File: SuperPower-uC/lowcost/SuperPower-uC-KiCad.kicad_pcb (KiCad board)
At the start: 2 copper layers, 81 x 28.5 mm, 81 parts, among them J1 Battery connector, J2 Thermistor, J3 USB_B_Micro, J4 Solar in, J5 main pin header fight, J6 main pin header left, Q1 2N7002, Q2 2N7002, Q3 S8050, Q4 S8050, Q5 AO3401A, Q6 AO3401A, Q7 2N7002, U1 FS312F-G, U10 FP6291LR, U11 ME6210A33P, U12 ME6210A33P, U13 ESP32-WROOM32, U2 FS8205A, U3 LC709203FQH, U4 TP4056, U5 CH340G, U6 AMS1117-3.3, U7 PCF8563T, U8 XC6206P332MR, U9 TCA6408A, Y1 12MHZ, Y2 32.768KHz

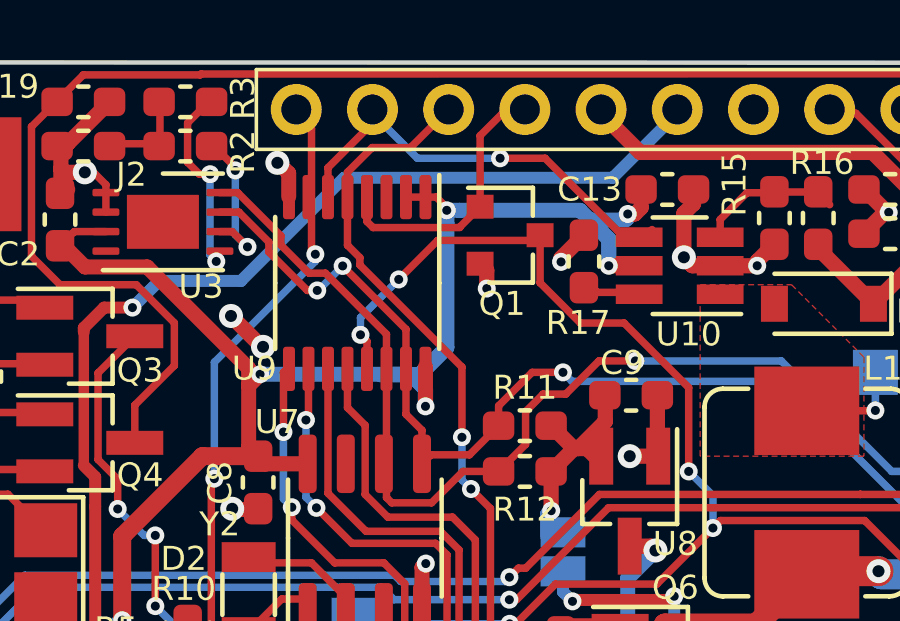
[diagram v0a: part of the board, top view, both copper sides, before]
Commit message: added pullup to pcb
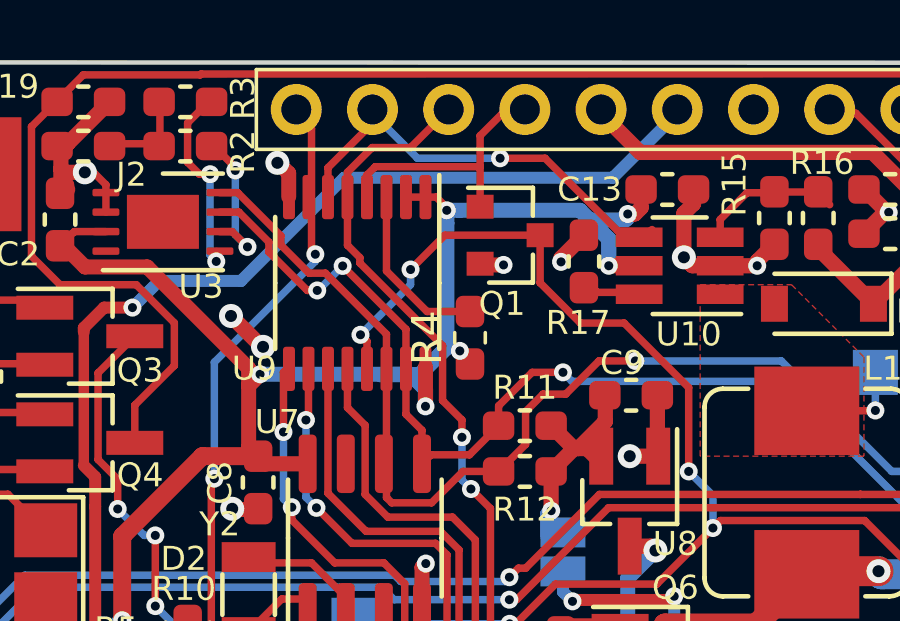
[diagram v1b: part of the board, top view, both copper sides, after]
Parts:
- added R4: 180k, Resistor_SMD:R_0603_1608Metric_Pad1.05x0.95mm_HandSolder, F.Cu at (136.5, 104.1)
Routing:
- net Net-(R4-Pad2): track 0.00 -> 5.81 mm
- net /Battery Module/VBAT: track 119.6 -> 120.6 mm, vias 15 -> 16

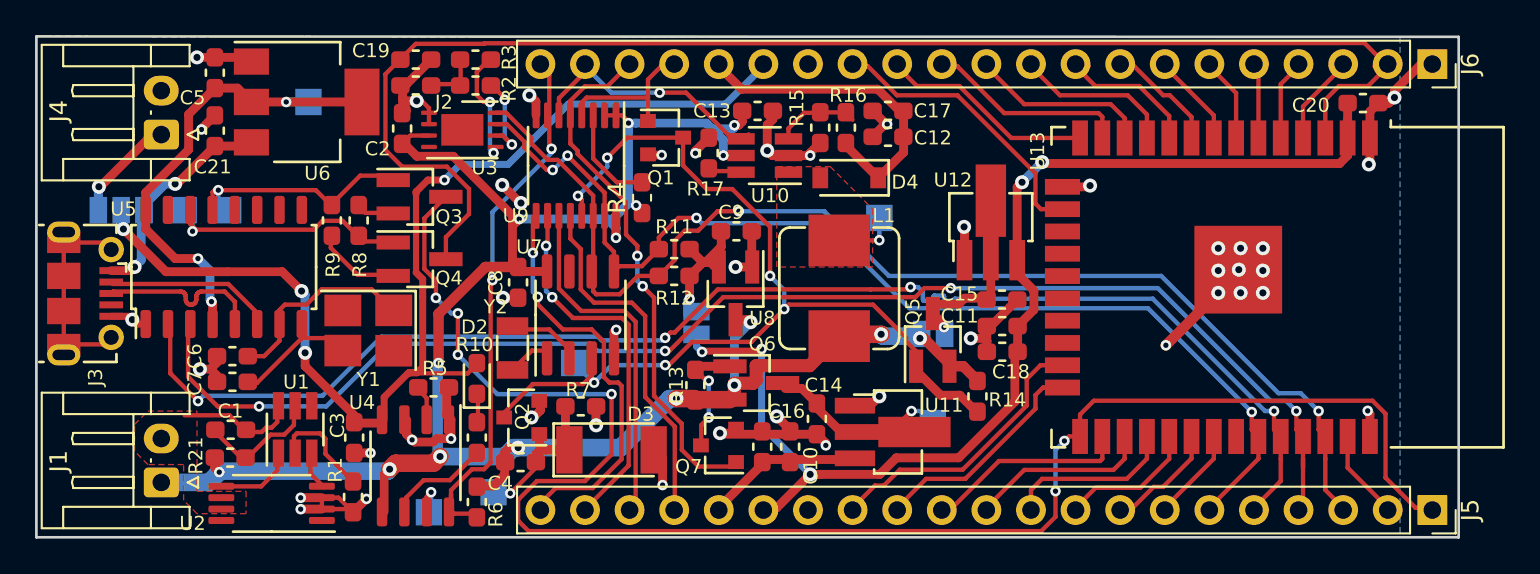
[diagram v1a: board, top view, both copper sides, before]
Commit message: connected vcci of io expander to vI2C
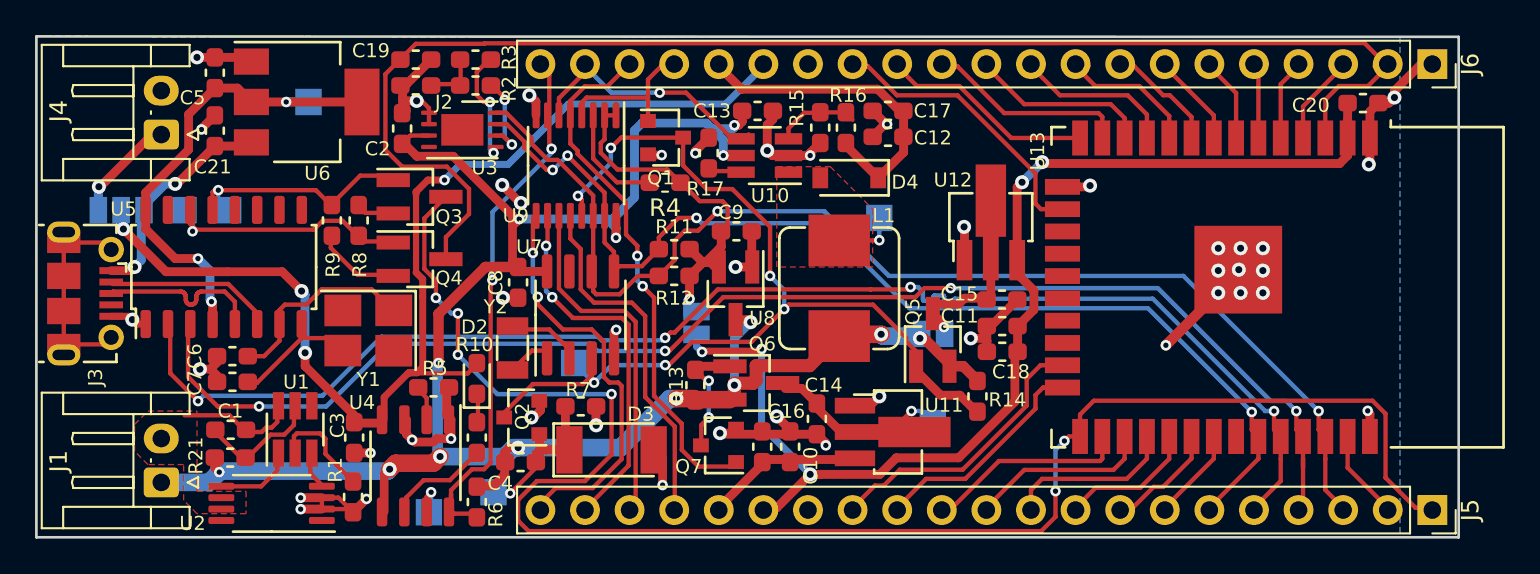
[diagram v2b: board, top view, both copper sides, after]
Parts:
- moved R4 1.56 mm to (137.8, 103.3), turned to 180 degrees
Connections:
- R4 pad 1: /Battery Module/VBAT -> /RTC and Cut-Off Module/V_I2C
- U9 pad 1: /Battery Module/VBAT -> /RTC and Cut-Off Module/V_I2C
- U9 pad 2: /Battery Module/VBAT -> /RTC and Cut-Off Module/V_I2C
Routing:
- net /RTC and Cut-Off Module/V_I2C: track 7.44 -> 20.4 mm
- net /Battery Module/VBAT: track 120.6 -> 117.5 mm, vias 16 -> 14

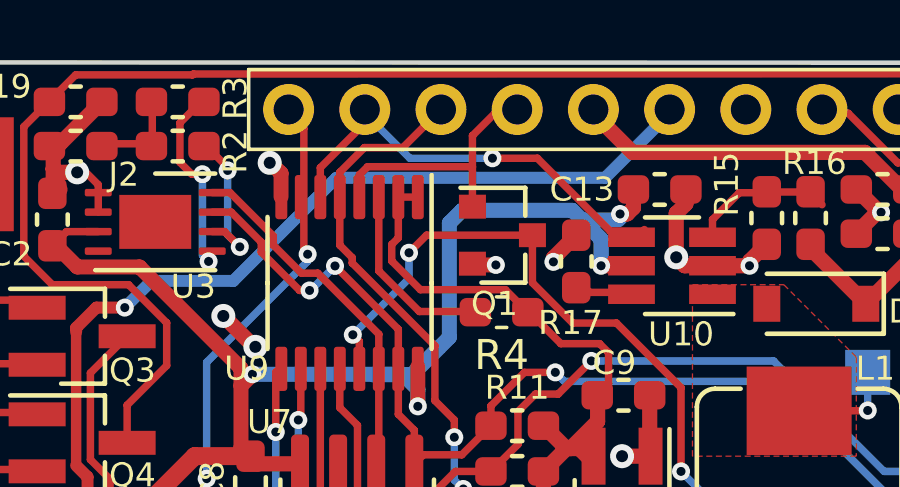
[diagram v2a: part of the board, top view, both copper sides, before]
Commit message: changed int io to directely connect to int bus
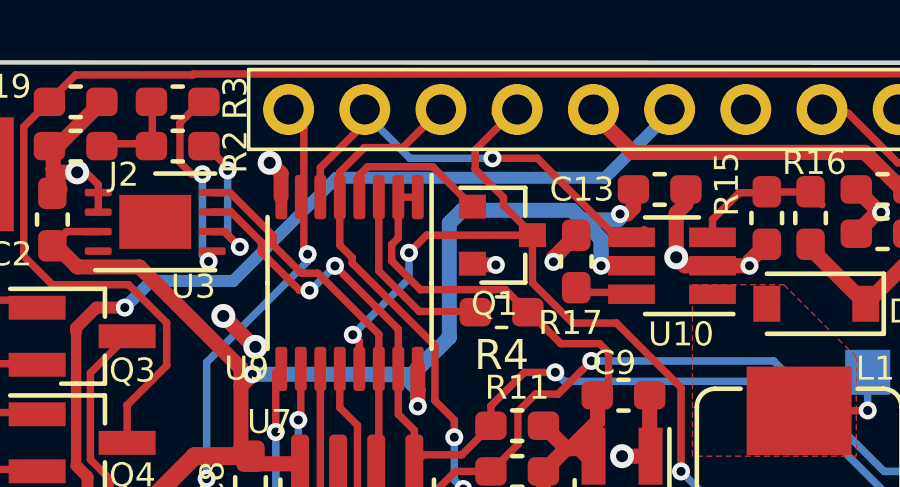
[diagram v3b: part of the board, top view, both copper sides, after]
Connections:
- Q1 pad 1: INT_IO -> Net-(Q1-Pad1)
- Q1 pad 3: /Charging Module/INT -> INT_IO
- Q2 pad 3: /Charging Module/INT -> INT_IO
- Q5 pad 1: /Charging Module/INT -> INT_IO
- R14 pad 2: /Charging Module/INT -> INT_IO
- TP2 pad 1: /Charging Module/INT -> INT_IO
- U7 pad 3: /Charging Module/INT -> INT_IO
- U9 pad 13: /Charging Module/INT -> INT_IO
- U9 pad 4: INT_IO -> Net-(Q1-Pad1)
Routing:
- net /Charging Module/INT: track 57.9 -> 0.00 mm, vias 6 -> 0
- net INT_IO: track 8.79 -> 64.2 mm, vias 0 -> 6
- net Net-(Q1-Pad1): track 0.00 -> 5.18 mm

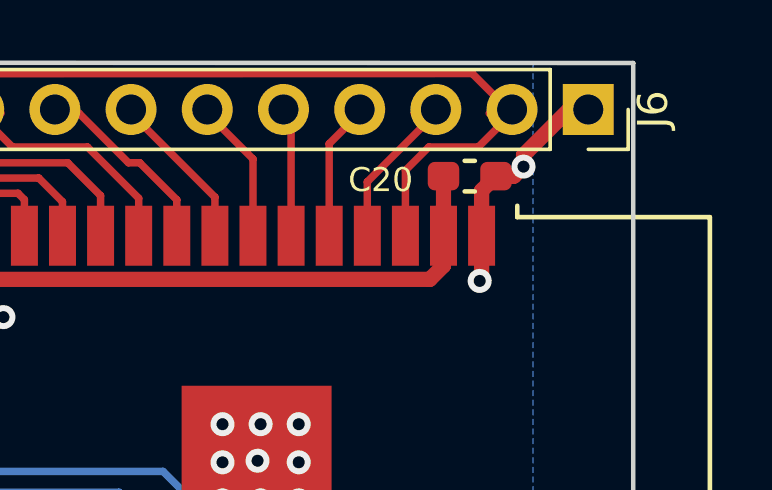
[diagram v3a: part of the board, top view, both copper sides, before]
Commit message: added rst pullup
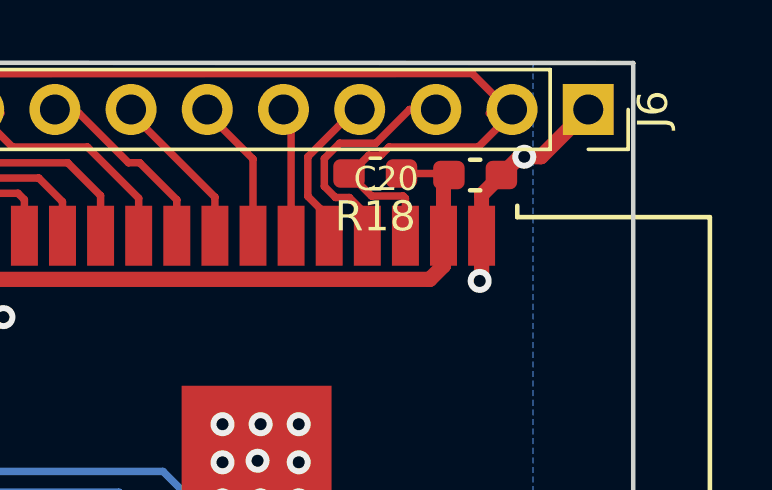
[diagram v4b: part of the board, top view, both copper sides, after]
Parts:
- added R18: 180k, Resistor_SMD:R_0603_1608Metric_Pad1.05x0.95mm_HandSolder, F.Cu at (174.4, 98.7)
- moved C20 0.18 mm to (177.7, 98.7)
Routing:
- net /Charger I/O/RST: track 80.8 -> 84.1 mm
- net /MCU Module/IO36: track 5.75 -> 7.83 mm
- net /MCU Module/3v3_MCU: track 65.9 -> 67.6 mm
- net /MCU Module/IO39: track 4.50 -> 5.26 mm

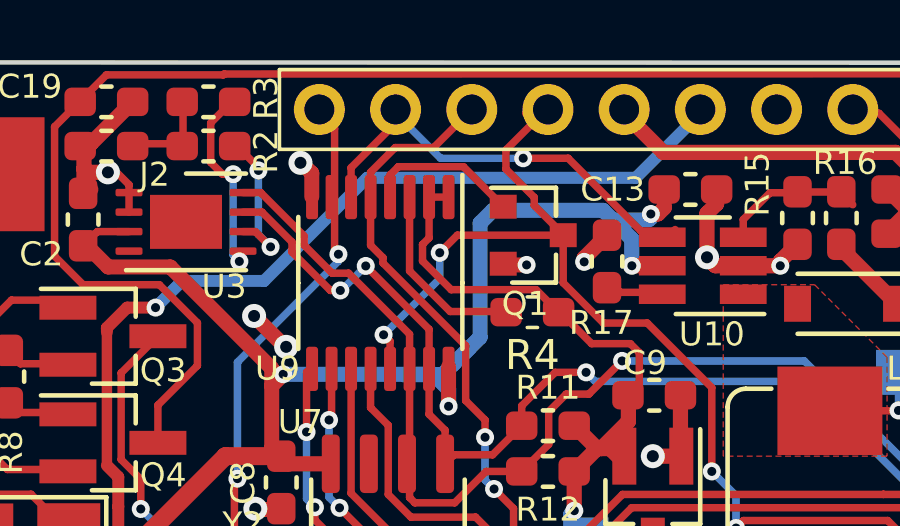
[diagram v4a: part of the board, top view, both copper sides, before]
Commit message: connected espander address pin to VBAT
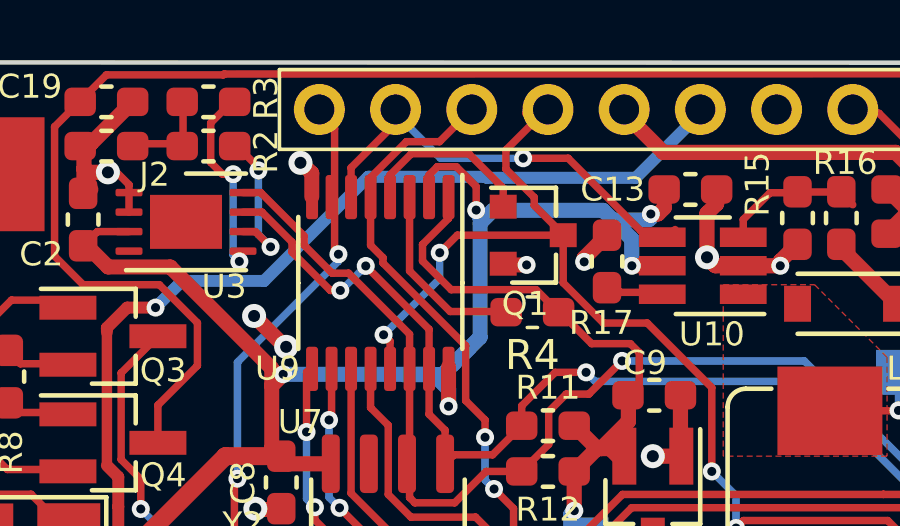
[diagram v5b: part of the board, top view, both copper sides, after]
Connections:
- U9 pad 2: /RTC and Cut-Off Module/V_I2C -> /Battery Module/VBAT
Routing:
- net /Battery Module/VBAT: track 117.5 -> 121.5 mm, vias 14 -> 15
- net Net-(Q1-Pad1): track 5.18 -> 5.90 mm

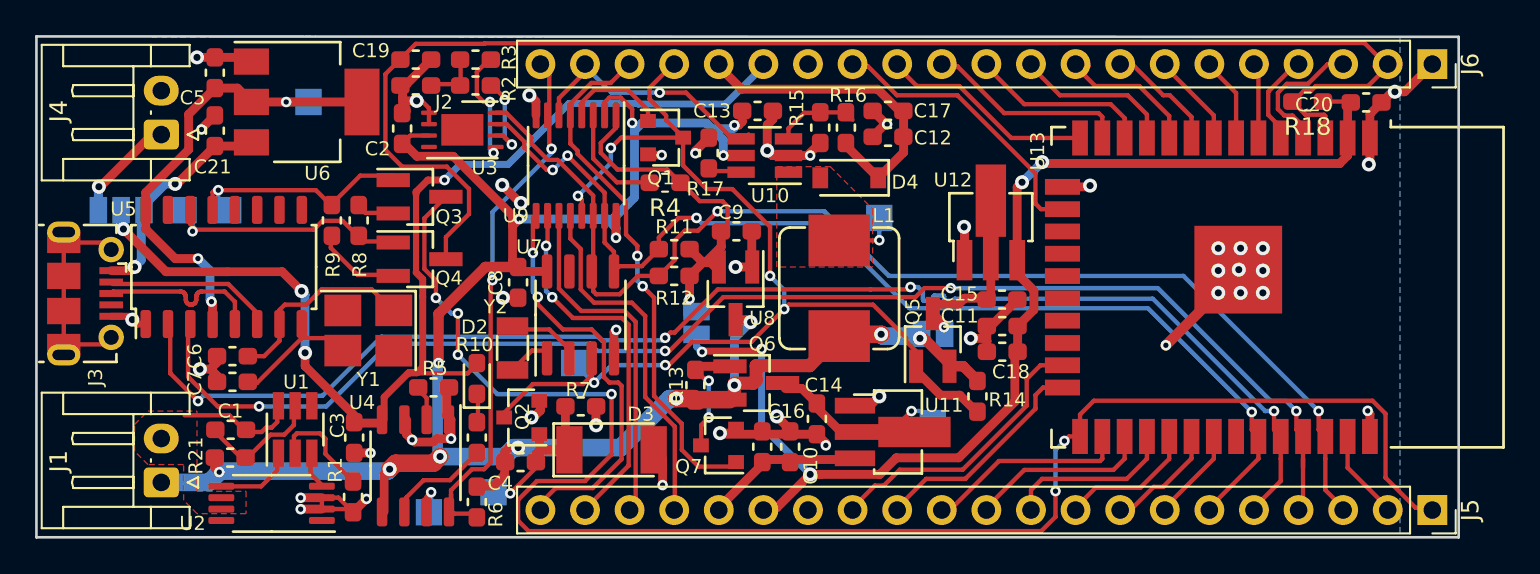
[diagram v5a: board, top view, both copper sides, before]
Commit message: connected vccd of io expander to 3v3 i2c and added bypass cap
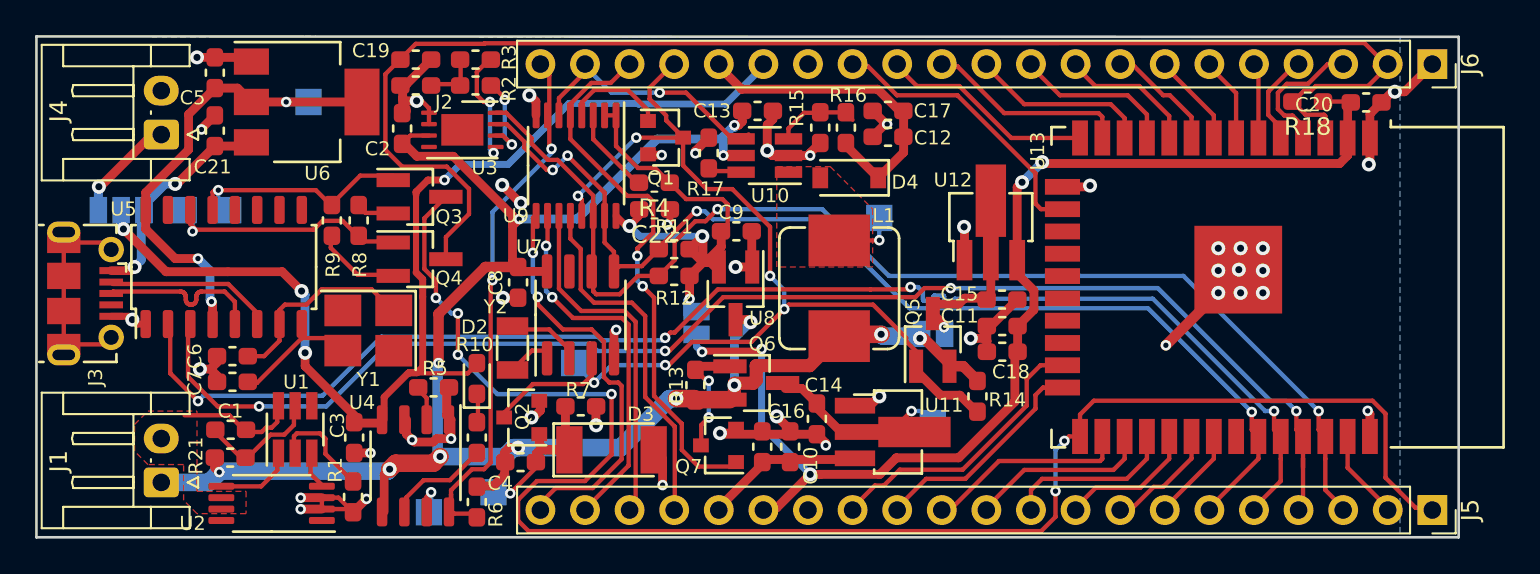
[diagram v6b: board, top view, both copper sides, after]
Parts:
- added C22: 0.1µF, Capacitor_SMD:C_0603_1608Metric_Pad1.05x0.95mm_HandSolder, F.Cu at (137.2, 104.8)
- moved R4 0.61 mm to (137.2, 103.3)
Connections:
- U9 pad 16: /Battery Module/VBAT -> /RTC and Cut-Off Module/V_I2C
- U9 pad 2: /Battery Module/VBAT -> /RTC and Cut-Off Module/V_I2C
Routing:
- net /Battery Module/VBAT: track 121.5 -> 110.8 mm, vias 15 -> 13
- net /RTC and Cut-Off Module/V_I2C: track 20.0 -> 28.4 mm, vias 1 -> 3
- net 3v3_EN: track 30.1 -> 31.6 mm
- net Net-(R4-Pad2): track 6.25 -> 4.99 mm
- net GND: track 88.3 -> 89.2 mm, vias 45 -> 46
- net INT_IO: track 64.2 -> 63.7 mm

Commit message: fixed auto reset transistor footprints
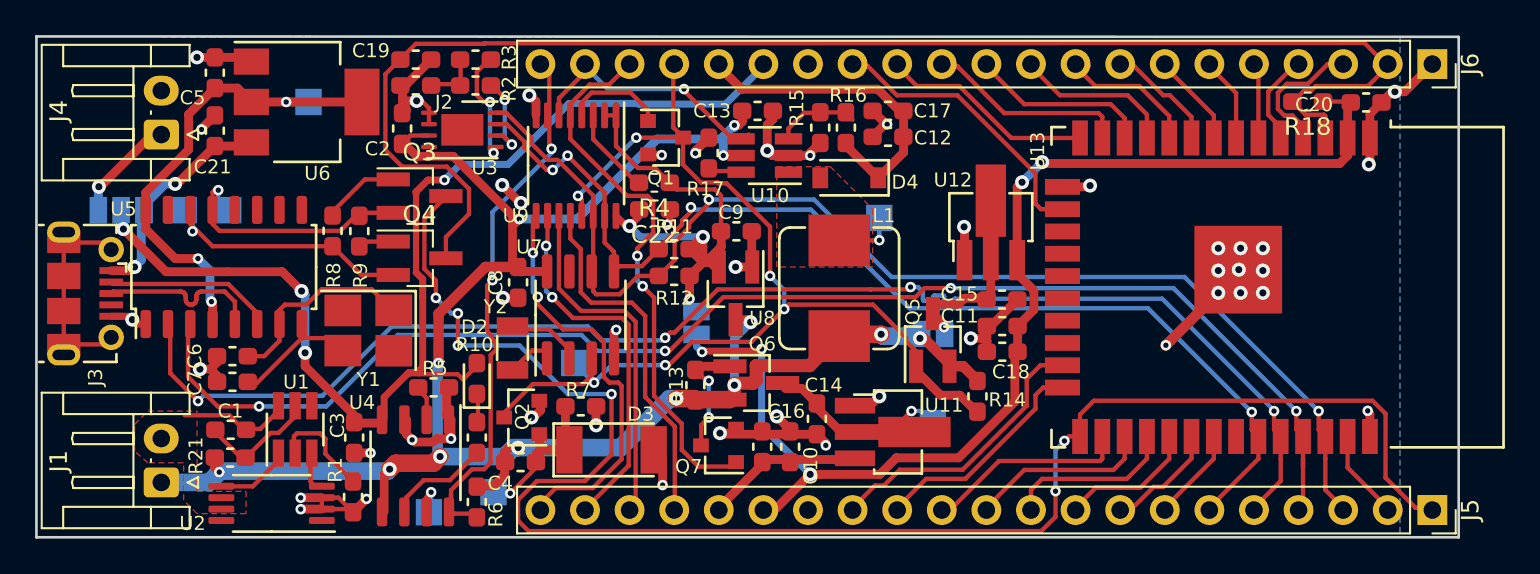
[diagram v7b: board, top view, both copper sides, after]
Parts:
- moved R9 1.68 mm to (120.4, 106.0)
- moved R8 1.60 mm to (118.8, 106.0)
- moved Q4 0.05 mm to (123.8, 107.6)
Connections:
- R8 pad 1: Net-(Q3-Pad2) -> Net-(Q3-Pad1)
- R8 pad 2: Net-(Q4-Pad1) -> Net-(Q4-Pad2)
- R9 pad 1: Net-(Q4-Pad2) -> Net-(Q4-Pad1)
- R9 pad 2: Net-(Q3-Pad1) -> Net-(Q3-Pad2)
- TP6 pad 1: Net-(Q4-Pad1) -> Net-(Q4-Pad2)
- TP7 pad 1: Net-(Q3-Pad1) -> Net-(Q3-Pad2)
- U5 pad 13: Net-(Q3-Pad1) -> Net-(Q3-Pad2)
- U5 pad 14: Net-(Q4-Pad1) -> Net-(Q4-Pad2)
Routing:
- net Net-(Q4-Pad1): track 14.6 -> 2.20 mm, vias 1 -> 0
- net Net-(Q3-Pad2): track 2.00 -> 14.4 mm, vias 0 -> 1
- net Net-(Q4-Pad2): track 4.56 -> 15.3 mm, vias 0 -> 1
- net Net-(Q3-Pad1): track 13.7 -> 4.43 mm, vias 1 -> 0
- net INT_IO: track 63.7 -> 62.6 mm
- net /Charging Module/SCL: track 68.8 -> 69.5 mm
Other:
- rule trace_min: 0.15 -> 0.25
